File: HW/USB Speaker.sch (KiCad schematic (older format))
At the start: 34 parts, among them J1 USB_OTG, U1 PCM2707C, Y1 12 MHz

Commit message: What did I do?
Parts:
- R?: value 1.5K -> 10K
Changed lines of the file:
@@
 	3850 5100 4000 5100
 Wire Wire Line
-	3850 5100 3850 5250
-Wire Wire Line
-	3850 5250 3850 5650
-Wire Wire Line
-	3850 5650 3850 5900
+	3850 5100 3850 5900
 Wire Wire Line
 	4350 5650 4250 5650
@@
 	4100 6350 4100 6250
 Wire Wire Line
-	3850 6250 4100 6250
-Wire Wire Line
-	4100 6250 4350 6250
+	3850 6250 4350 6250
 Wire Wire Line
 	3850 6250 3850 6200
@@
 Connection ~ 4100 6250
 Wire Wire Line
-	4350 5100 4350 5250
-Wire Wire Line
-	4350 5250 4350 5650
-Wire Wire Line
-	4350 5650 4350 5900
-Wire Wire Line
-	7750 3600 7750 4150
-Wire Wire Line
-	7750 4150 7750 4200
-Wire Wire Line
-	7750 4200 7750 4300
-Wire Wire Line
-	7750 4150 7850 4150
-Wire Wire Line
-	7850 4150 8100 4150
-Wire Wire Line
-	7850 3600 7850 3650
-Wire Wire Line
-	7850 3650 7850 3700
+	4350 5100 4350 5900
+Wire Wire Line
+	7750 3600 7750 4300
+Wire Wire Line
+	7750 4150 8100 4150
+Wire Wire Line
+	7850 3600 7850 3700
 Wire Wire Line
 	7850 4150 7850 4000
@@
 	7450 3000 7350 3000
 Wire Wire Line
-	5400 3000 5650 3000
-Wire Wire Line
-	5650 3000 7100 3000
-Wire Wire Line
-	7100 3000 7150 3000
+	5400 3000 7150 3000
 Wire Wire Line
 	7100 3700 7100 3000
@@
 	7100 4200 7750 4200
 Wire Wire Line
-	3600 1800 3800 1800
-Wire Wire Line
-	3800 1800 4400 1800
-Wire Wire Line
-	4400 1800 4600 1800
-Wire Wire Line
-	4600 1800 5050 1800
+	3600 1800 5050 1800
 Wire Wire Line
 	3600 1800 3600 2500
@@
 Connection ~ 3800 1800
 Wire Wire Line
-	1650 2750 1650 3000
-Wire Wire Line
-	1650 3000 1650 3200
-Wire Wire Line
-	1650 3200 1650 3350
+	1650 2750 1650 3350
 Wire Wire Line
 	1900 3200 1650 3200
@@
 	4800 5100 5400 5100
 Wire Wire Line
-	5400 4900 5400 5100
-Wire Wire Line
-	5400 5100 5400 5200
+	5400 4900 5400 5200
 Wire Wire Line
 	2200 3200 2800 3200
@@
 	5400 5600 5400 5500
 Wire Wire Line
-	6300 3550 6300 3650
-Wire Wire Line
-	6300 3650 6300 3700
+	6300 3550 6300 3700
 Wire Wire Line
 	6300 3650 6050 3650
@@
 	6050 3800 6050 4050
 Wire Wire Line
-	6300 4000 6300 4050
-Wire Wire Line
-	6300 4050 6300 4100
+	6300 4000 6300 4100
 Wire Wire Line
 	6050 4050 6300 4050
@@
 	5400 3400 5500 3400
 Wire Wire Line
-	5800 3200 5900 3200
-Wire Wire Line
-	5900 3200 7450 3200
+	5800 3200 7450 3200
 Wire Wire Line
 	5800 3400 5900 3400
@@
 	4000 850  4000 2500
 Wire Wire Line
-	4000 850  6200 850
-Wire Wire Line
-	6200 850  7150 850
-Wire Wire Line
-	7150 850  7550 850
+	4000 850  7550 850
 Wire Wire Line
 	4200 1100 4200 2500
 Wire Wire Line
-	4200 1100 6650 1100
-Wire Wire Line
-	6650 1100 7350 1100
-Wire Wire Line
-	7350 1100 7550 1100
-Wire Wire Line
-	7850 850  8200 850
-Wire Wire Line
-	8200 850  9400 850
-Wire Wire Line
-	7850 1100 8400 1100
-Wire Wire Line
-	8400 1100 9400 1100
+	4200 1100 7550 1100
+Wire Wire Line
+	7850 850  9400 850
+Wire Wire Line
+	7850 1100 9400 1100
 Wire Wire Line
 	6200 1200 6200 850
@@
 	3800 5450 3800 4900
 Wire Wire Line
-	2100 5450 2600 5450
-Wire Wire Line
-	2600 5450 3800 5450
+	2100 5450 3800 5450
 Wire Wire Line
 	2800 3400 2050 3400
@@
 	2050 3950 750  3950
 Wire Wire Line
-	750  3800 750  3950
-Wire Wire Line
-	750  3950 750  4050
+	750  3800 750  4050
 $Comp
 L R R13
@@
 S 7450 4800 1850 1450
 U 5B317E48
-F0 "Better Power Circuit" 60
-F1 "Bettery_Power_Circuit.sch" 60
+F0 "Battery Power Circuit" 60
+F1 "Battery_Power_Circuit.sch" 60
 F2 "SSPNDn" I L 7450 5050 60
 $EndSheet
@@
 P 2600 5200
 F 0 "R?" V 2680 5200 50  0000 C CNN
-F 1 "1.5K" V 2600 5200 50  0000 C CNN
+F 1 "10K" V 2600 5200 50  0000 C CNN
 F 2 "" V 2530 5200 50  0001 C CNN
 F 3 "" H 2600 5200 50  0001 C CNN

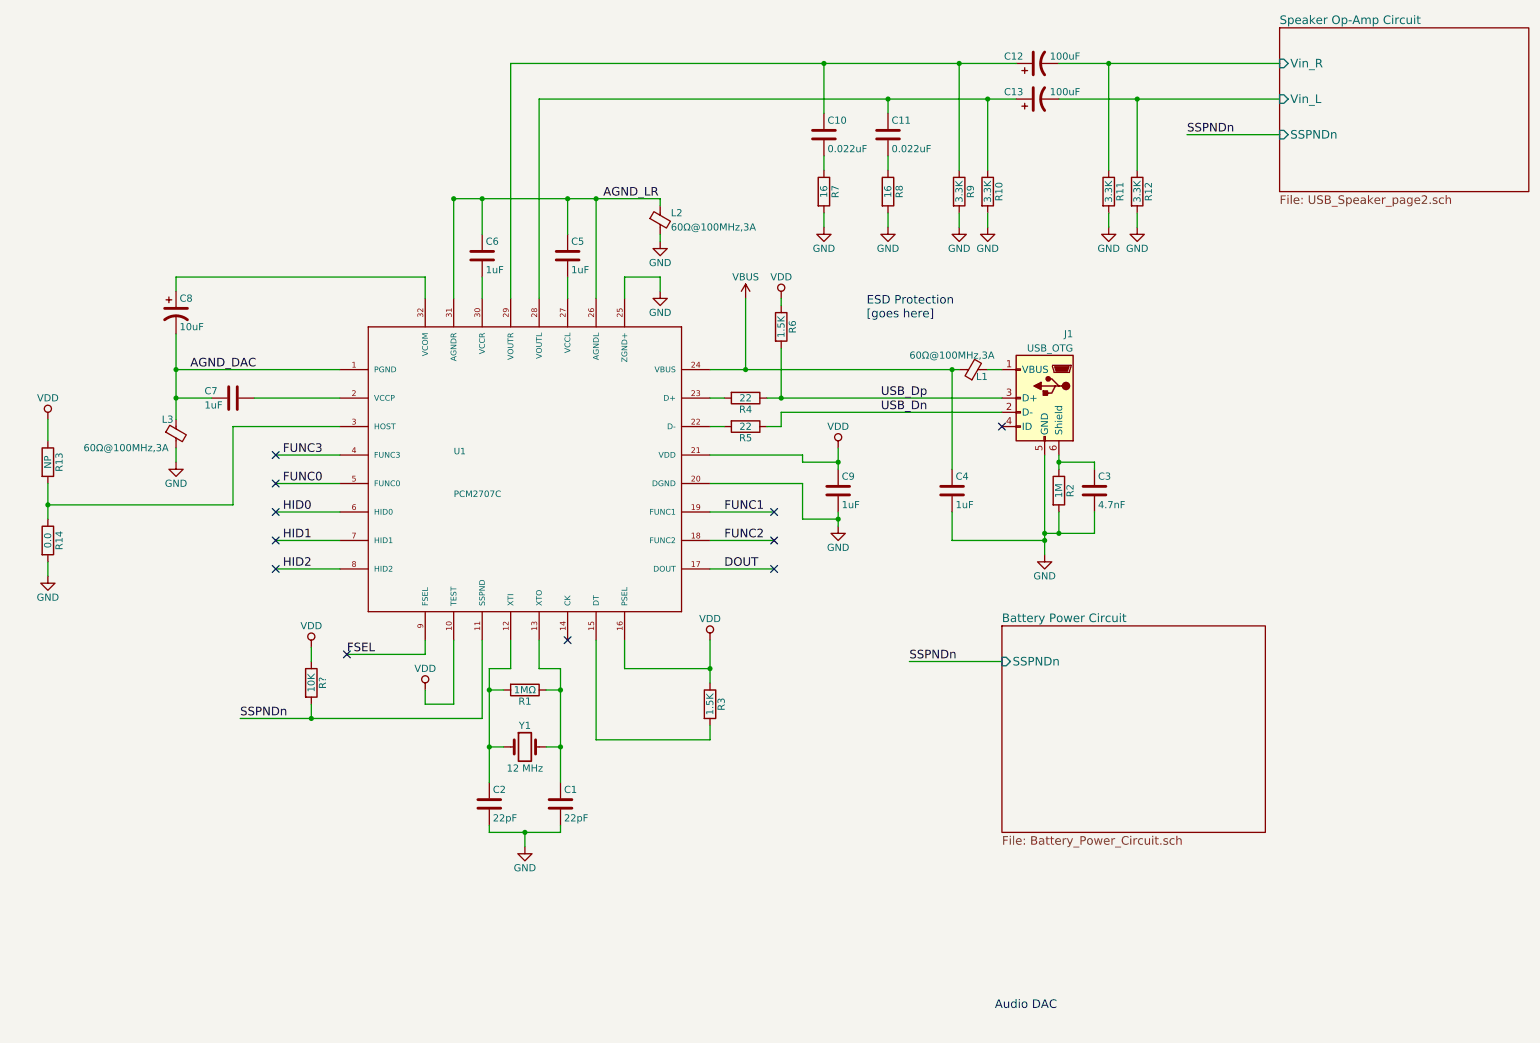
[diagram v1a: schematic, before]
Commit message: Added LEDs, Test points, and ESD protection on USB
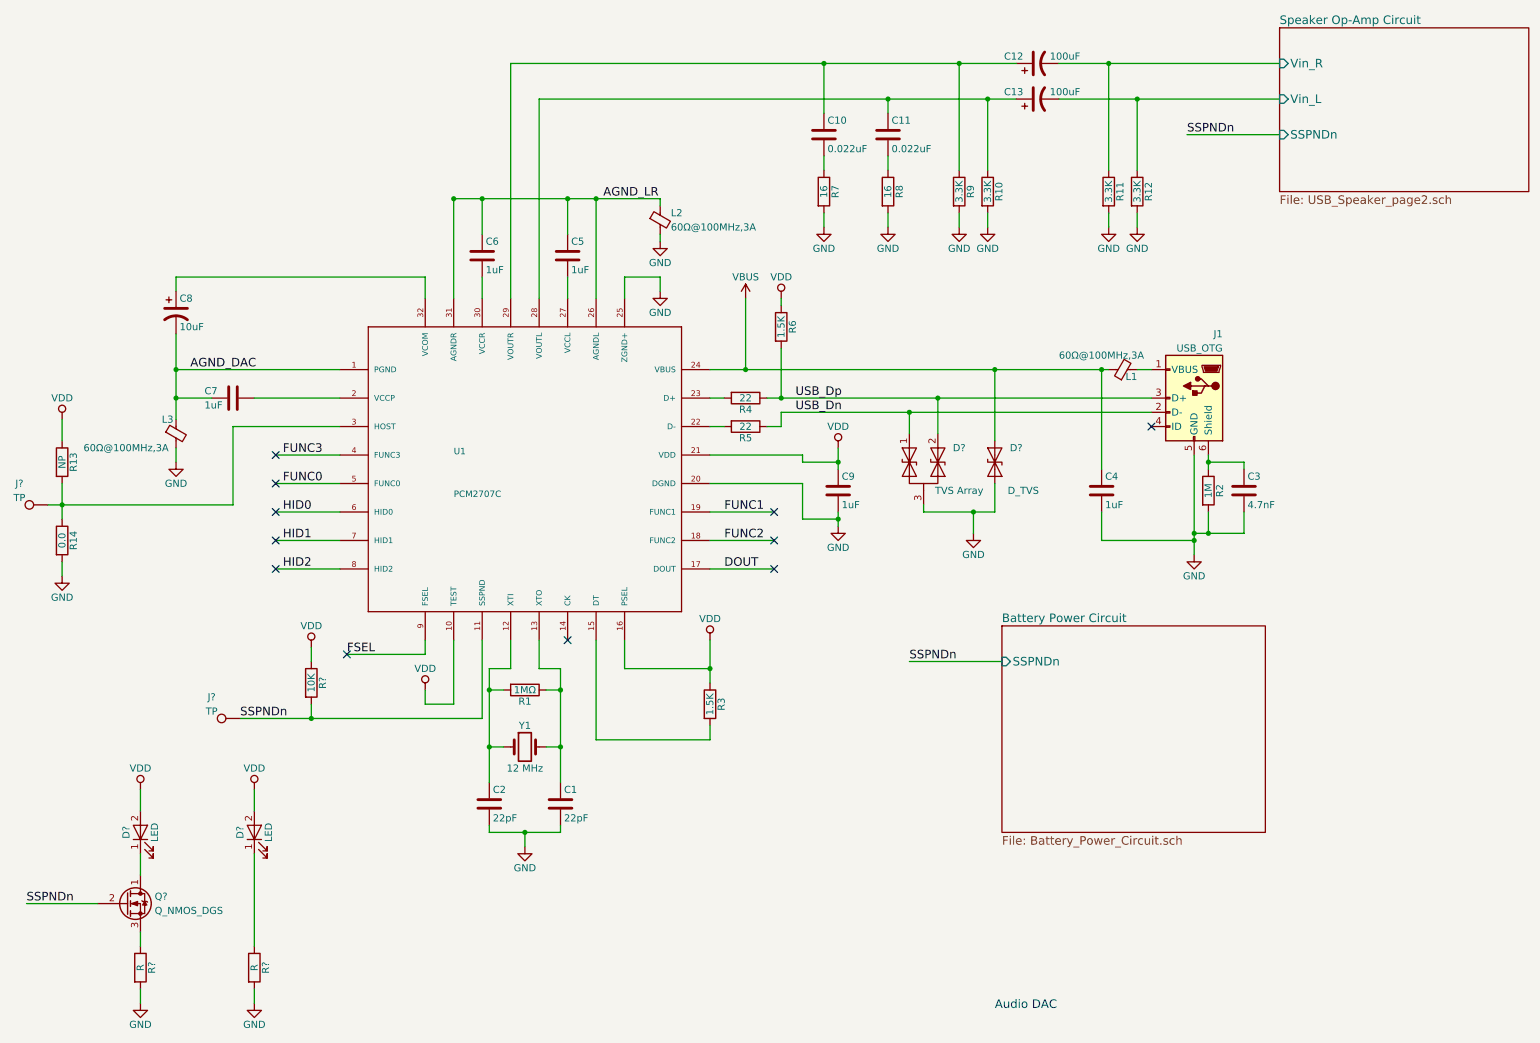
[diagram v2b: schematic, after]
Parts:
- added D? (x2): LED, symbol LED
- added D?: TVS Array, symbol D_TVS_x2_AAC_ALT
- added D?: D_TVS, symbol D_TVS
- added J? (x2): TP, symbol TEST_1P
- added Q?: Q_NMOS_DGS, symbol Q_NMOS_DGS
- added R? (x2): R, symbol R
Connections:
- net GND: now also D?.1 (A1), D?.3 (common), R?.2, R?.2
- net SSPNDn: now also J?.1, Q?.2 (G)
- net USB_Dn: now also D?.1 (A1)
- net USB_Dp: now also D?.2 (A2)
- net VBUS: now also D?.2 (A2)
- net VDD: now also D?.2 (A), D?.2 (A)
- net at R13.2, R14.1, U1.3 (HOST): now also J?.1
- new net: D?.1 (K), Q?.1 (D)
- new net: Q?.3 (S), R?.1
- new net: D?.1 (K), R?.1
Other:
- note removed: "ESD Protection\n[goes here]\n"
- moved on the sheet: C3, C4, J1, L1, R13, R14, R2

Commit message: First draft done :100:
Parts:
- removed C1, C2: 22pF, symbol C
- removed C10, C11: 0.022uF, symbol C
- removed C12, C13: 100uF, symbol CP1
- removed D?: D_TVS, symbol D_TVS
- removed J?: TP, symbol TEST_1P
- removed Q?: Q_NMOS_DGS, symbol Q_NMOS_DGS
- removed R12: 3.3K, symbol R
- removed R5: 22, symbol R
- removed R?: 10K, symbol R
- removed R?: R, symbol R
- added C1, C2: 100uF, symbol CP1
- added C12, C13: 22pF, symbol C
- added C3, C4: 0.022uF, symbol C
- added D1: D_TVS, symbol D_TVS
- added J3: TP, symbol TEST_1P
- added Q1: Q_NMOS_DGS, symbol Q_NMOS_DGS
- added R17: R, symbol R
- added R2: 16, symbol R
- added R3, R6: 3.3K, symbol R
- R10: value 3.3K -> NP
- R13: value NP -> 10K
- R4: value 22 -> 3.3K
- R8: value 16 -> 22
- R9: value 3.3K -> 22
- gave numbers to parts that had none: 5
- renumbered C4 to C10, C3 to C11, C8 to C7, C7 to C8, L2 to L1, L1 to L2, R7 to R1, R2 to R11, R14 to R12, R1 to R14, R3 to R15, R11 to R5, R6 to R7
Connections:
- net GND: now also R4.2, C12.2, C13.2, D1.1 (A1), R17.2, R2.2, R3.2, R6.2; no longer R10.2, R8.2, R9.2
- net SSPNDn: now also R13.2, J3.1, Q1.2 (G)
- net Speaker Op-Amp Circuit/Vin_L: now also C2.2, R6.1
- net Speaker Op-Amp Circuit/Vin_R: now also C1.2
- net USB_Dn: now also R9.1
- net USB_Dp: now also R8.1; no longer R4.1
- net VBUS: now also D1.2 (A2)
- net VDD: now also R10.1
- net at R14.2, U1.12 (XTI), Y1.1: now also C12.1
- net at R14.1, U1.13 (XTO), Y1.2: now also C13.1
- net at U1.22 (D-): now also R9.2
- net at U1.23 (D+): now also R8.2; no longer R4.2
- net at U1.27 (VCCL): now also C6.2; no longer C5.2
- net at U1.28 (VOUTL): now also R4.1, C2.1, C4.1; no longer R10.1
- net at U1.29 (VOUTR): now also C1.1, C3.1, R3.1; no longer R9.1
- net at J2.1, R12.1, U1.3 (HOST): now also R10.2; no longer R13.2
- net at U1.30 (VCCR): now also C5.2; no longer C6.2
- net at R1.1: now also C3.2
- net at D3.1 (K): now also Q1.1 (D)
- net at R16.1: now also Q1.3 (S)
- net at D4.1 (K): now also R17.1
- new net: C4.2, R2.1
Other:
- note added: "LED Power???\n"

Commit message: First :b:raft 4realz :100:
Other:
- note removed: "LED Power???\n"
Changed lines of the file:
@@
 	6800 3450 6800 3300
 Connection ~ 6800 3300
-Text Notes 2500 6800 0    60   ~ 0
-LED Power???\n
 $Sheet
 S 4900 6300 1500 1150
